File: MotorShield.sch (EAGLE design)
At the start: 119 parts, among them IC1 OPA4340E, IC2 OPA4340E, IC3 74HCT125D, T1 FDN337N, T2 FDN337N, T3 FDN337N, T4 FDN337N, T5 FDN337N, T6 FDN337N, T7 FDN337N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

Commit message: completely changed wiring of GPIOs https://github.com/IUNO-TDM/PumpControl/issues/27 https://github.com/IUNO-TDM/MotorShield/issues/11
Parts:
- added R57: 10k, rcl:R-EU_R0805
- added R58, R59, R60: 220, rcl:R-EU_R0805
- T9: value BC847C -> FDN337N; device transistor:BC847C-NPN-SOT23-BEC -> zetex:NMOSSOT23
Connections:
- removed net CLK: IC3A.I, PCB1.GPIO11/SCLK, U$1.SCK
- removed net DIN: IC3B.I, PCB1.GPIO10/MOSI, U$1.MOSI
- removed net DOUT: PCB1.GPIO09/MISO, U$1.MISO
- removed net SPI0CE1: IC3A.OE, IC3B.OE
- new net BTN_LED: PCB1.GEN5/GPIO24, R57.2, T9.G
- new net GPIO07: PCB1.!CE!/GPIO07
- new net GPIO08: PCB1.!CE0!/GPIO08
- new net GPIO10: PCB1.GPIO10/MOSI
- new net GPIO11: PCB1.GPIO11/SCLK
- new net N$60: R59.2, X4.-4
- new net N$61: R60.2, X4.-6
- new net PWM0: PCB1.GPIO12
- new net PWM1: PCB1.GPIO13
- new net RXD0: PCB1.RXD0/GPIO15
- new net SPI1_CE2: PCB1.GPIO16
- new net SPI1_MISO: PCB1.GPIO19, U$1.MISO
- new net SPI1_MOSI: IC3B.I, PCB1.GPIO20, U$1.MOSI
- new net SPI1_SCLK: IC3A.I, PCB1.GPIO21, U$1.SCK
- new net TXD0: PCB1.TXD0/GPIO14
- net CS_ADC: now also PCB1.GPIO18; no longer PCB1.!CE0!/GPIO08
- net CS_DOTSTARS: now also IC3A.OE, IC3B.OE, PCB1.GPIO17/GEN0; no longer PCB1.!CE!/GPIO07
- net GND: now also R57.1, R58.1, R59.1, R60.1, T9.S; no longer T9.E, X4.-2, X4.-4, X4.-6
- net INP_BTN_START: now also PCB1.GPIO04/GCKL
- net INP_DOOR_CTRL: now also PCB1.GEN4/GPIO23
- net INP_DOOR_JUICE: now also PCB1.GPIO22/GEN3
- net M1: now also PCB1.GPIO06; no longer PCB1.GPIO13
- net M2: now also PCB1.GPIO05; no longer PCB1.GPIO06
- net M3: no longer PCB1.GPIO05
- net M4: no longer PCB1.GPIO22/GEN3
- net M5: no longer PCB1.GEN4/GPIO23
- net M6: now also PCB1.GPIO09/MISO; no longer PCB1.GPIO17/GEN0
- net M7: now also PCB1.GEN6/GPIO25; no longer PCB1.GPIO04/GCKL
- net N$32: now also T9.D; no longer T9.C
- net N$33: now also R58.2, X4.-2; no longer T9.B
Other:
- note removed: "SPI1 MISO"
- note removed: "SPI1 MOSI"
- note removed: "SPI1 SCLK"
- moved on the sheet: X4

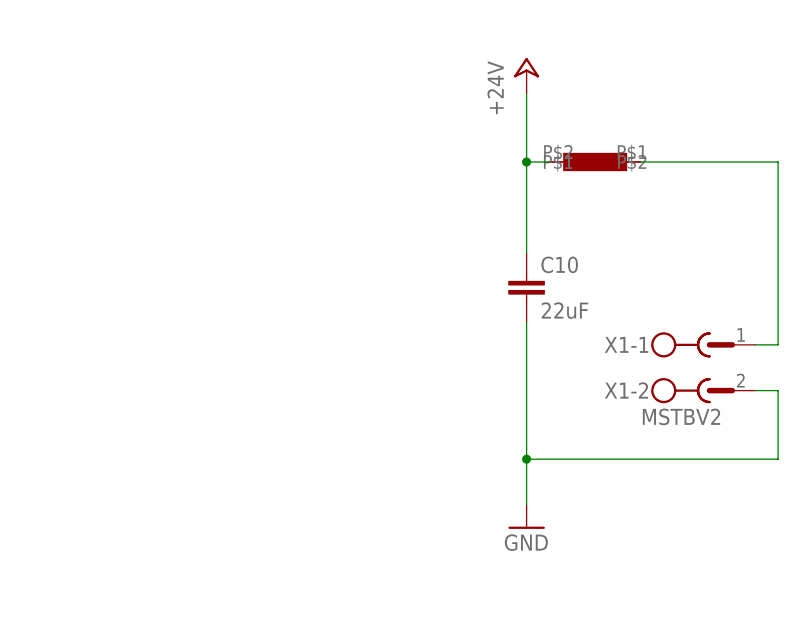
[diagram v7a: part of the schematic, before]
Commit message: added power indicator led
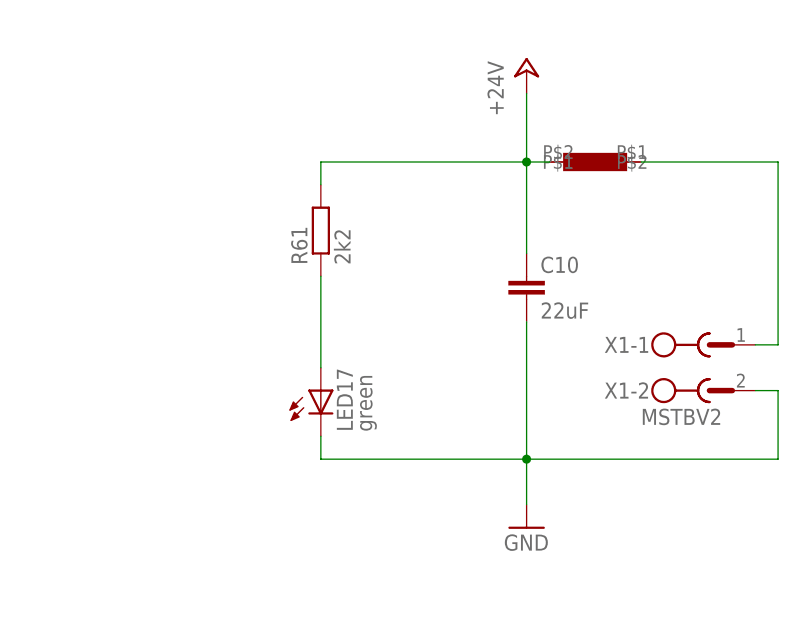
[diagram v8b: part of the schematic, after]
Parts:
- added LED17: green, led:LEDCHIP-LED0805
- added R61: 2k2, rcl:R-EU_R0805
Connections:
- new net N$62: LED17.A, R61.1
- net +24V: now also R61.2
- net GND: now also LED17.C
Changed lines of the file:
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@@
 <part name="R59" library="rcl" deviceset="R-EU_" device="R0805" value="220"/>
 <part name="R60" library="rcl" deviceset="R-EU_" device="R0805" value="220"/>
+<part name="LED17" library="led" deviceset="LED" device="CHIP-LED0805" value="green"/>
+<part name="R61" library="rcl" deviceset="R-EU_" device="R0805" value="2k2"/>
 </parts>
 <sheets>
@@
 <instance part="R59" gate="G$1" x="124.46" y="190.5"/>
 <instance part="R60" gate="G$1" x="129.54" y="185.42"/>
+<instance part="LED17" gate="G$1" x="464.82" y="137.16"/>
+<instance part="R61" gate="G$1" x="464.82" y="154.94" rot="R90"/>
 </instances>
 <busses>
@@
 <pinref part="GND5" gate="1" pin="GND"/>
 <wire x1="487.68" y1="124.46" x2="487.68" y2="129.54" width="0.1524" layer="91"/>
+<pinref part="LED17" gate="G$1" pin="C"/>
+<wire x1="464.82" y1="132.08" x2="464.82" y2="129.54" width="0.1524" layer="91"/>
+<wire x1="464.82" y1="129.54" x2="487.68" y2="129.54" width="0.1524" layer="91"/>
 </segment>
 <segment>
@@
 <pinref part="C10" gate="G$1" pin="1"/>
 <wire x1="487.68" y1="152.4" x2="487.68" y2="162.56" width="0.1524" layer="91"/>
+<pinref part="R61" gate="G$1" pin="2"/>
+<wire x1="464.82" y1="160.02" x2="464.82" y2="162.56" width="0.1524" layer="91"/>
+<wire x1="464.82" y1="162.56" x2="487.68" y2="162.56" width="0.1524" layer="91"/>
 </segment>
 <segment>
@@
 </segment>
 </net>
+<net name="N$62" class="0">
+<segment>
+<pinref part="LED17" gate="G$1" pin="A"/>
+<pinref part="R61" gate="G$1" pin="1"/>
+<wire x1="464.82" y1="139.7" x2="464.82" y2="149.86" width="0.1524" layer="91"/>
+</segment>
+</net>
